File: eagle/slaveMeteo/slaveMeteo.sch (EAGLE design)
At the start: 20 parts, among them J1 RJ12RIGHTANGLE-I2C, U3 ATMEGA328, X1 1503_09

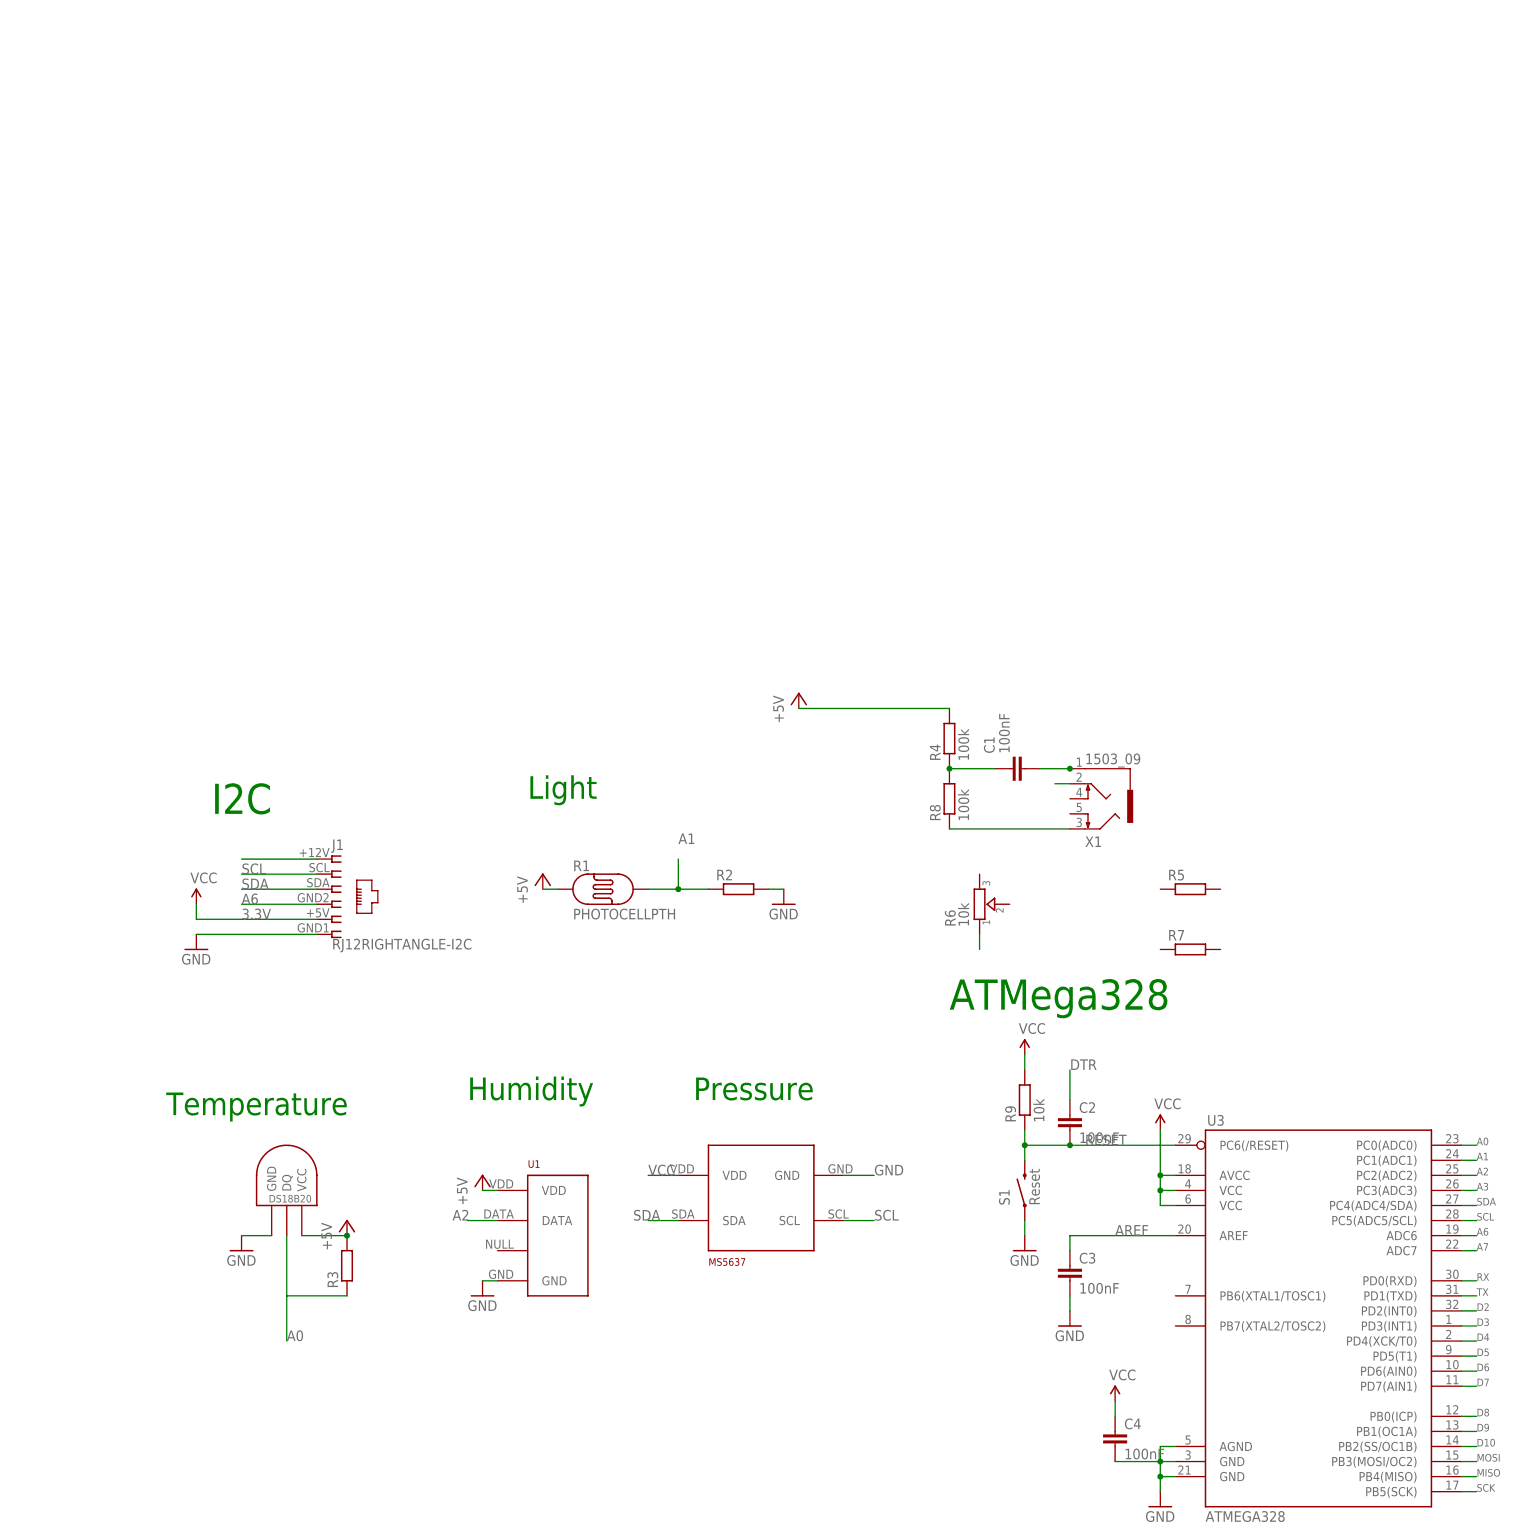
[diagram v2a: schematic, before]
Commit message: redesigned meteoSlave using slave-basic
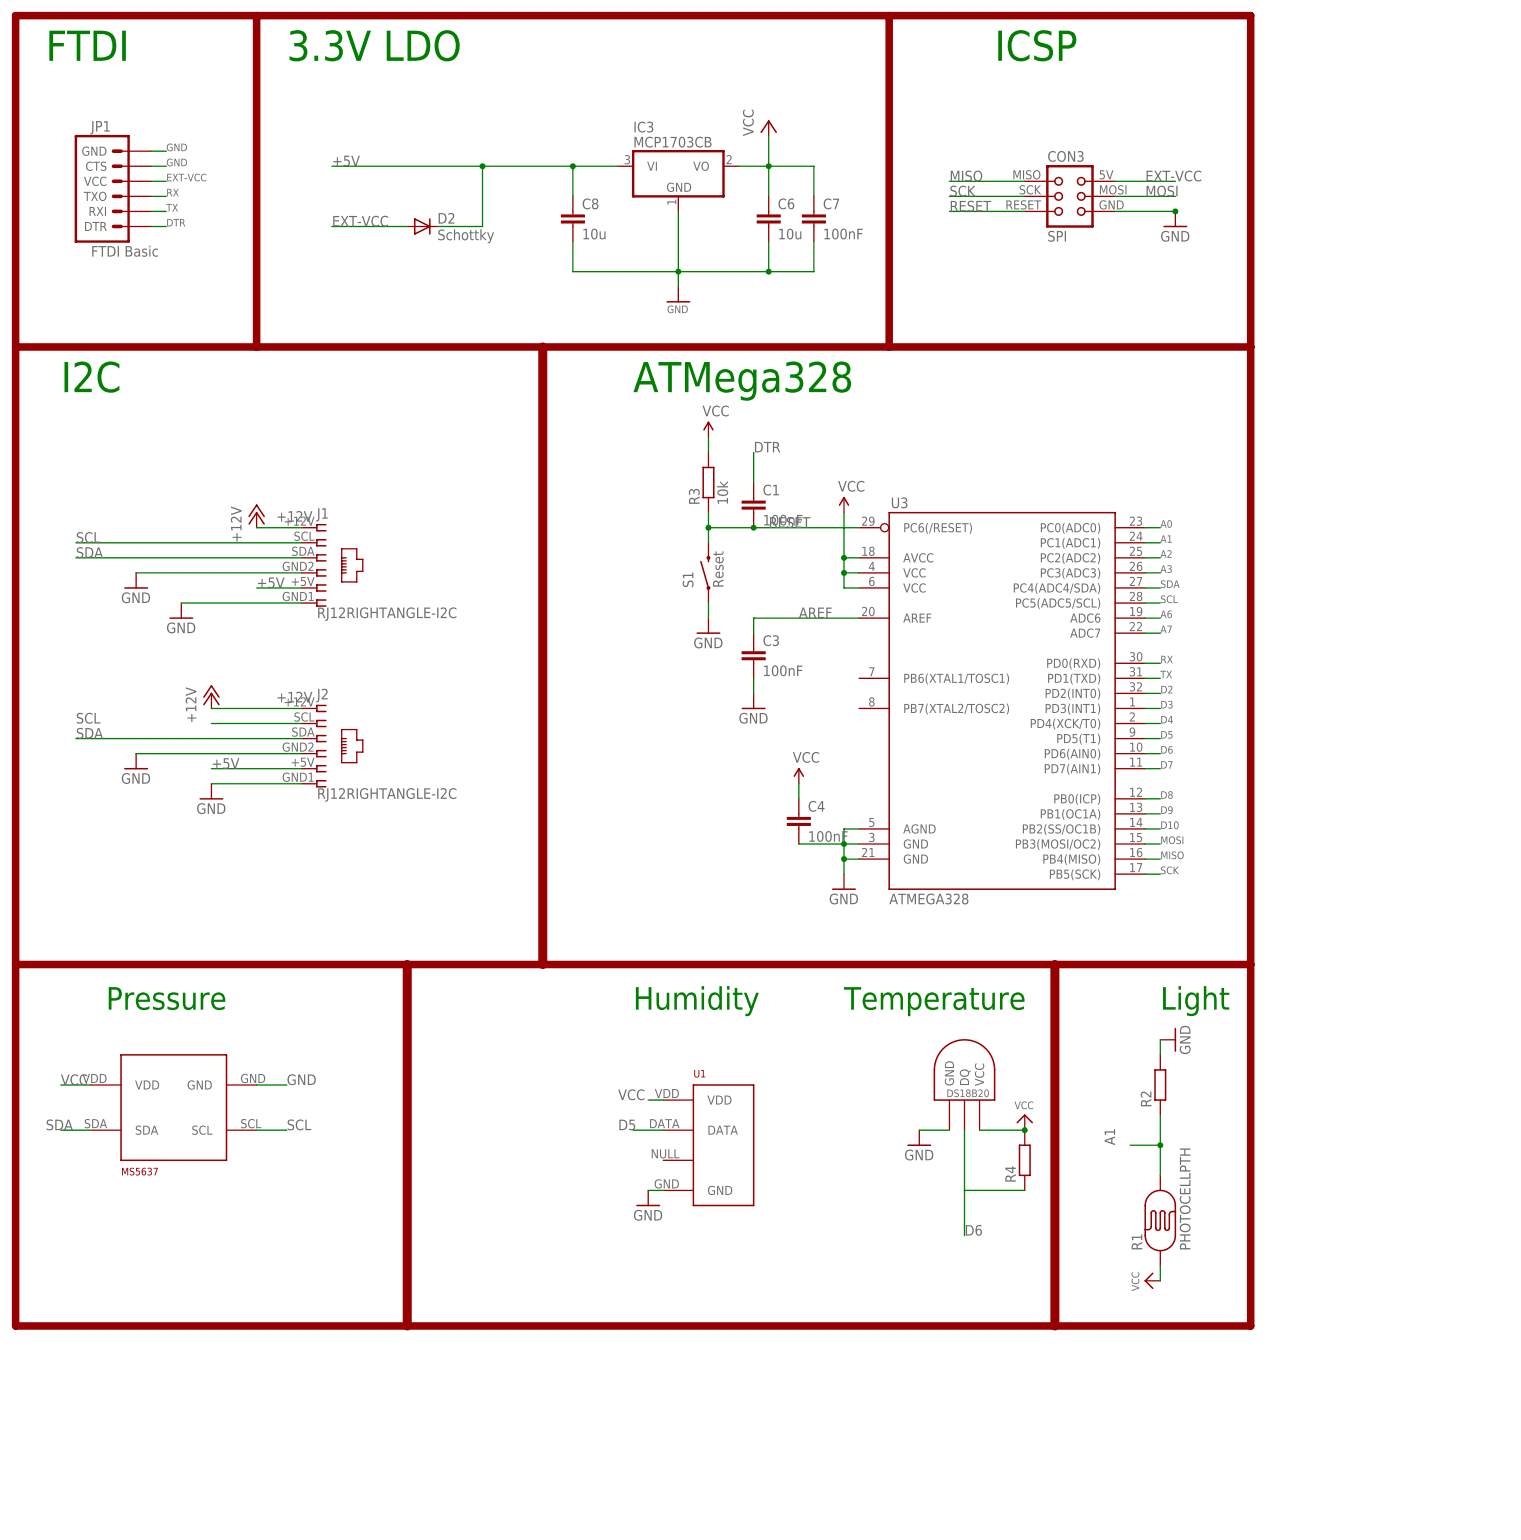
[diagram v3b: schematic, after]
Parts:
- removed C2: 100nF, rcl:C-EUC0805K
- removed R5, R7: (no value), resistor:R-EU_R0805
- removed R6: 10k, dp_devices:TRIMMER-3362P
- removed R8: 100k, resistor:R-EU_R0805
- removed R9: 10k, rcl:R-EU_R0805
- removed X1: 1503_09, con-lumberg:1503_09
- added C6, C8: 10u, rcl:C-EUC0805K
- added C7: 100nF, rcl:C-EUC0805K
- added CON3: SPI, lpatiny:TINYISPTAG
- added D2: Schottky, diode:MBR0520LT
- added IC3: MCP1703CB, linear:MCP1703CB
- added J2: RJ12RIGHTANGLE-I2C, lpatiny:RJ12RIGHTANGLE-I2C
- added JP1: FTDI Basic, SparkFun:ARDUINO_SERIAL_PROGRAMPTH
- C1: device dp_devices:CAPACITOR_NPOL-0805 -> rcl:C-EUC0805K; ELECROW (none) -> C49678; LCSC (none) -> C49678; MPN (none) -> 80-C1206C104K5R
- R3: value (none) -> 10k; device resistor:R-EU_R0805 -> rcl:R-EU_R0805; ELECROW (none) -> C17513; LCSC (none) -> C17513
- R4: value 100k -> (none)
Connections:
- removed net 3.3V: J1.5
- removed net GND1: R6.1
- removed net GND2: R8.1, X1.3
- removed net N$14: C1.2, X1.1
- removed net N$21: X1.2
- removed net N$4: J1.1
- removed net N$5: C1.1, R4.1, R8.2
- new net +12V: J1.1, J2.1
- new net EXT-VCC: CON3.VCC, D2.A, JP1.VCC
- net +5V: now also C8.1, D2.C, IC3.VI, J1.5, J2.5; no longer R1.P$1, R3.2, R4.2, U$1.VCC, U1.VDD
- net A0: no longer R3.1, U$1.DQ
- net A2: no longer U1.DATA
- net A6: no longer J1.4
- net D5: now also U1.DATA
- net D6: now also R4.1, U$1.DQ
- net DTR: now also C1.1, JP1.DTR; no longer C2.1
- net GND: now also C6.2, C7.2, C8.2, CON3.GND, IC3.GND, J1.4, J2.4, J2.6, JP1.CTS, JP1.GND
- net MISO: now also CON3.MISO
- net MOSI: now also CON3.MOSI
- net RESET: now also C1.2, CON3.RESET, R3.1; no longer C2.2, R9.1
- net RX: now also JP1.TXO
- net SCK: now also CON3.SCK
- net SCL: now also J2.2
- net SDA: now also J2.3
- net TX: now also JP1.RXI
- net VCC: now also C6.1, C7.1, IC3.VO, R1.P$1, R3.2, R4.2, U$1.VCC, U1.VDD; no longer R9.2
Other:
- note added: "3.3V LDO"
- note added: "FTDI"
- note added: "ICSP"
- moved on the sheet: C3, C4, J1, R1, R2, R3, R4, S1, U1, U3
